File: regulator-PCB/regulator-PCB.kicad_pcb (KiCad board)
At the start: 2 copper layers, 92 parts, among them J1 Conn_ARM_SWD_TagConnect_TC2030, J2 PJ-059A, J3 Conn_01x01_Pin, J4 Conn_01x01_Pin, J5 Conn_01x01_Pin, J6 Conn_01x01_Pin, J7 Conn_01x01_Pin, Q1 2N3904, Q10 2N3904, Q11 2N3904, Q12 2N3904, Q13 2N3904, Q14 2N3904, Q15 2N3904, Q2 2N3904, Q3 2N3904, Q4 2N3904, Q5 2N3904, Q6 2N3904, Q7 2N3904, Q8 2N3904, Q9 2N3904, U1 STM32C092KCT6, U10 LH1546AT, U11 LH1546AT, U12 LH1546AT, U13 LH1546AT, U14 LH1546AT, U15 LH1546AT, U16 LH1546AT, U17 LH1546AT, U2 LP2985-3.3, U3 LH1546AT, U4 LH1546AT, U5 LH1546AT, U6 LH1546AT, U7 LH1546AT, U8 LH1546AT, U9 LH1546AT

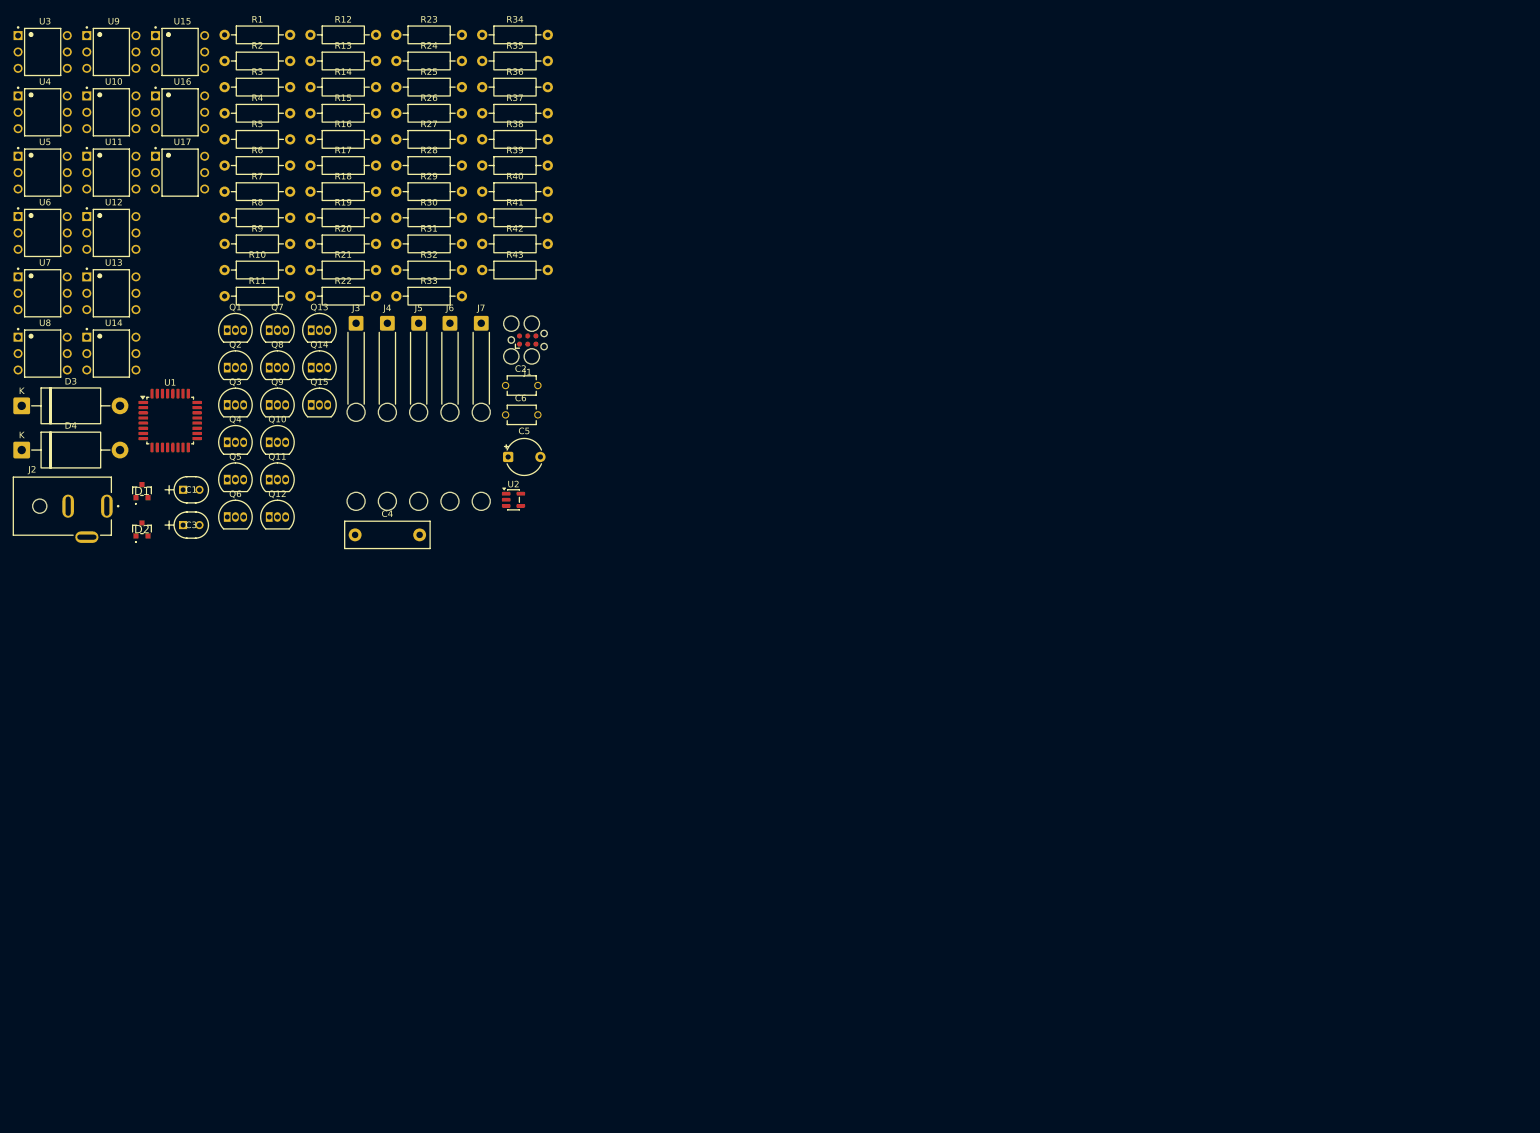
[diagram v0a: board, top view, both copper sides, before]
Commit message: Regular PCB schematic completed. Drafted a poor design for the regulator PCB, then added line voltage safety constraints. Pending PCB redesign.
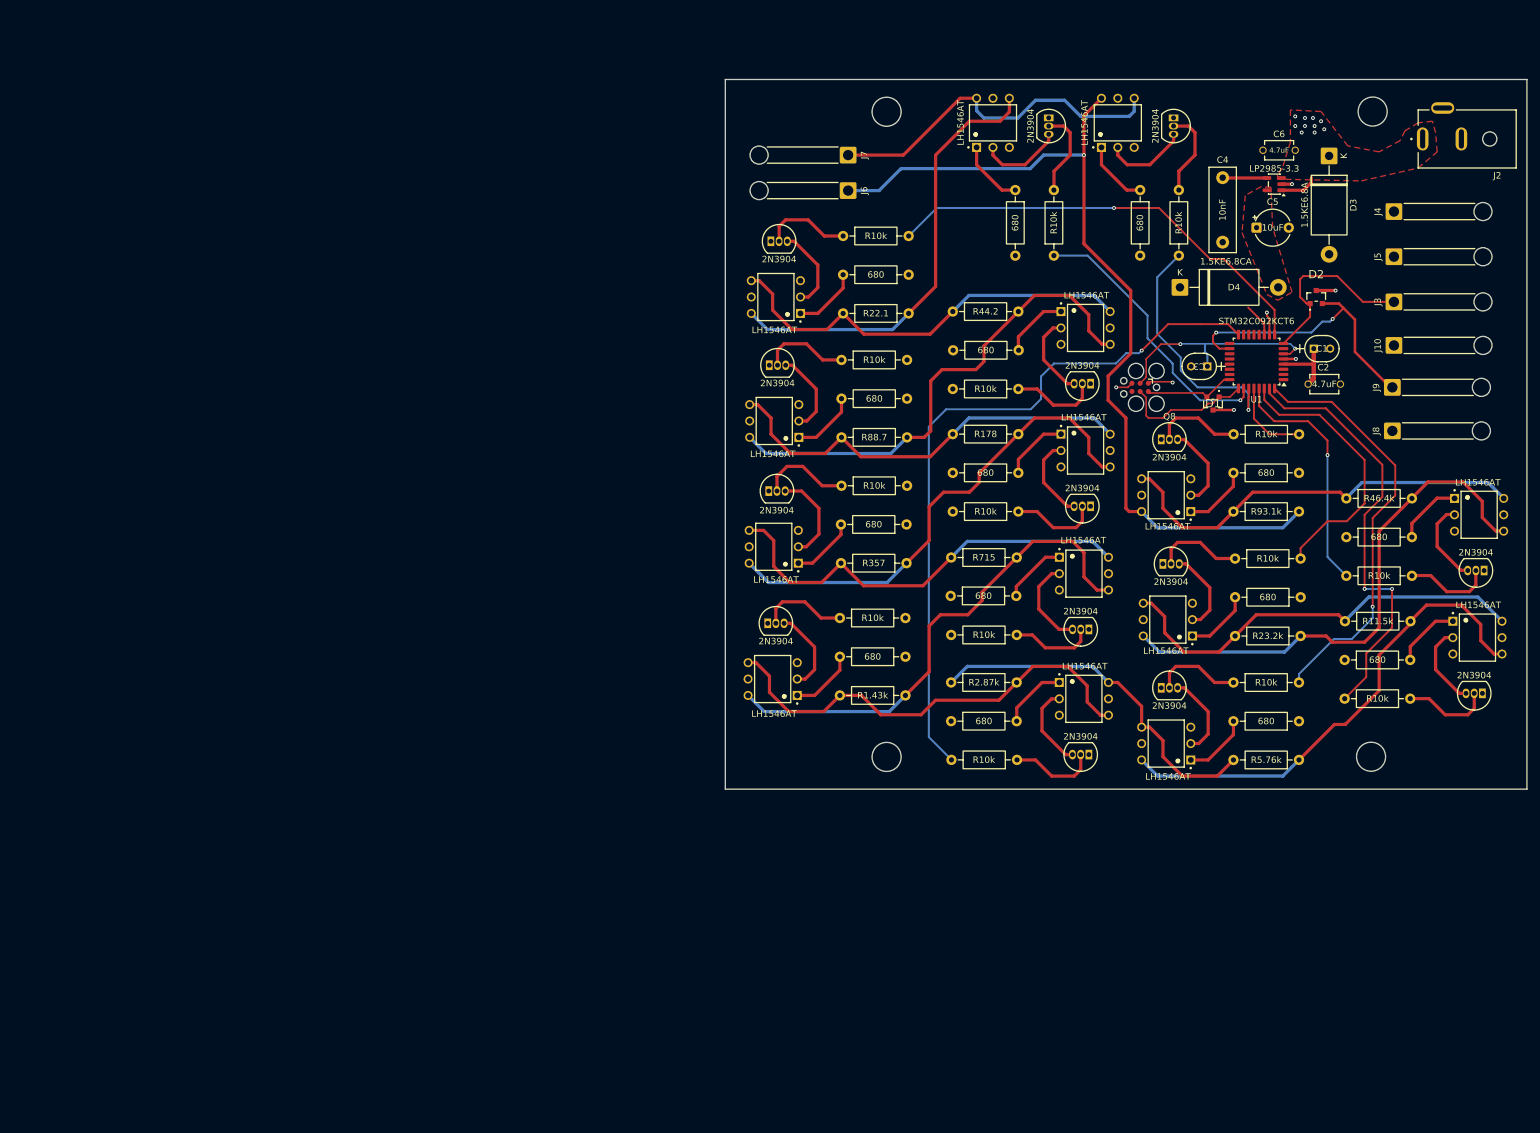
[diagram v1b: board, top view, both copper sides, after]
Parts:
- added H1: MountingHole, MountingHole:MountingHole_4.5mm, F.Cu at (229.2, 130.2)
- added H2: MountingHole, MountingHole:MountingHole_4.5mm, F.Cu at (229.5, 30.2)
- added H3: MountingHole, MountingHole:MountingHole_4.5mm, F.Cu at (154.2, 30.3)
- added H4: MountingHole, MountingHole:MountingHole_4.5mm, F.Cu at (154.2, 130.3)
- added J10: Conn_01x01_Pin, Connector_Wire:SolderWire-0.75sqmm_1x01_D1.25mm_OD2.3mm_Relief, F.Cu at (232.8, 66.5)
- added J8: Conn_01x01_Pin, Connector_Wire:SolderWire-0.75sqmm_1x01_D1.25mm_OD2.3mm_Relief, F.Cu at (232.6, 79.8)
- added J9: Conn_01x01_Pin, Connector_Wire:SolderWire-0.75sqmm_1x01_D1.25mm_OD2.3mm_Relief, F.Cu at (232.6, 73.0)
- J3, J4, J5, J6, J7: footprint Connector_Wire:SolderWire-0.5sqmm_1x01_D0.9mm_OD2.3mm_Relief2x -> Connector_Wire:SolderWire-0.75sqmm_1x01_D1.25mm_OD2.3mm_Relief
- moved U11 218.5 mm to (246.0, 92.8)
- moved U13 218.4 mm to (245.7, 111.8)
- moved J2 211.7 mm to (237.2, 34.5), turned to 180 degrees
- moved D3 206.3 mm to (222.8, 37.1), turned to -90 degrees
- moved Q11 190.9 mm to (246.5, 120.4), turned to 180 degrees
- moved Q9 190.0 mm to (246.8, 101.4), turned to 180 degrees
- moved D2 185.5 mm to (220.8, 59.0)
- moved R26 181.5 mm to (235.3, 121.2), turned to 180 degrees
- moved D4 181.3 mm to (199.6, 57.5)
- moved C1 176.6 mm to (220.4, 67.0)
- moved U12 174.4 mm to (197.8, 109.0), turned to 180 degrees
- moved U14 174.3 mm to (197.5, 128.2), turned to 180 degrees
- moved U10 173.9 mm to (197.5, 89.7), turned to 180 degrees
- moved U15 172.3 mm to (184.7, 121.3)
- moved R28 169.8 mm to (235.6, 102.2), turned to 180 degrees
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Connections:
- net /ResInput renamed /Line-R-In
- net /ResOut renamed /Line-R-Out
- net Net-(R11-Pad1) renamed /Line-R3
- net Net-(R11-Pad2) renamed /Line-R4
- net Net-(R12-Pad2) renamed /Line-R5
- net Net-(R16-Pad2) renamed /Line-R6
- net Net-(R20-Pad2) renamed /Line-R7
- net Net-(R21-Pad2) renamed /Line-R8
- net Net-(R3-Pad1) renamed /Line-R1
- net Net-(R3-Pad2) renamed /Line-R2
- net Net-(R36-Pad1) renamed /Line-R9
- net Net-(R37-Pad1) renamed /Line-R10
- net Net-(R38-Pad1) renamed /Line-R11
- net Net-(R39-Pad1) renamed /Line-R12
- net Net-(R40-Pad1) renamed /Line-R13
- D2 pad 2: unconnected-(D2-A/K_2-Pad2) -> /rotary-encoder-output
- U1 pad 18: unconnected-(U1-PA8-Pad18) -> /rotary-encoder-output
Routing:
- net +5V: track 0.00 -> 271.5 mm, vias 0 -> 10
- net /Line-R-In: track 0.00 -> 138.2 mm, vias 0 -> 1
- net /Bit7: track 0.00 -> 110.4 mm, vias 0 -> 1
- net /Line-R12: track 0.00 -> 82.0 mm
- net /Line-R7: track 0.00 -> 78.1 mm
- net /Line-R3: track 0.00 -> 77.6 mm
- net /Line-R5: track 0.00 -> 76.3 mm
- net /Line-R10: track 0.00 -> 76.0 mm
- net /Line-R8: track 0.00 -> 70.5 mm
- net /Line-R1: track 0.00 -> 69.1 mm
- net /Bit0: track 0.00 -> 68.9 mm, vias 0 -> 1
- net /Line-R6: track 0.00 -> 67.9 mm
- net /Bit9: track 0.00 -> 67.5 mm, vias 0 -> 2
- net /Line-R4: track 0.00 -> 66.3 mm
- net /Line-R11: track 0.00 -> 66.2 mm
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- added copper zone on F.Cu, net +3.3V
- added copper zone on F.Cu, net +5V
- added copper zone on In2.Cu, net +5V
- added copper zone on In1.Cu, net GND
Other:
- board outline added: 124.2 x 110 mm
- copper layers 2 -> 4

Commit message: Regulator PCB v1.0 designed and ordered.
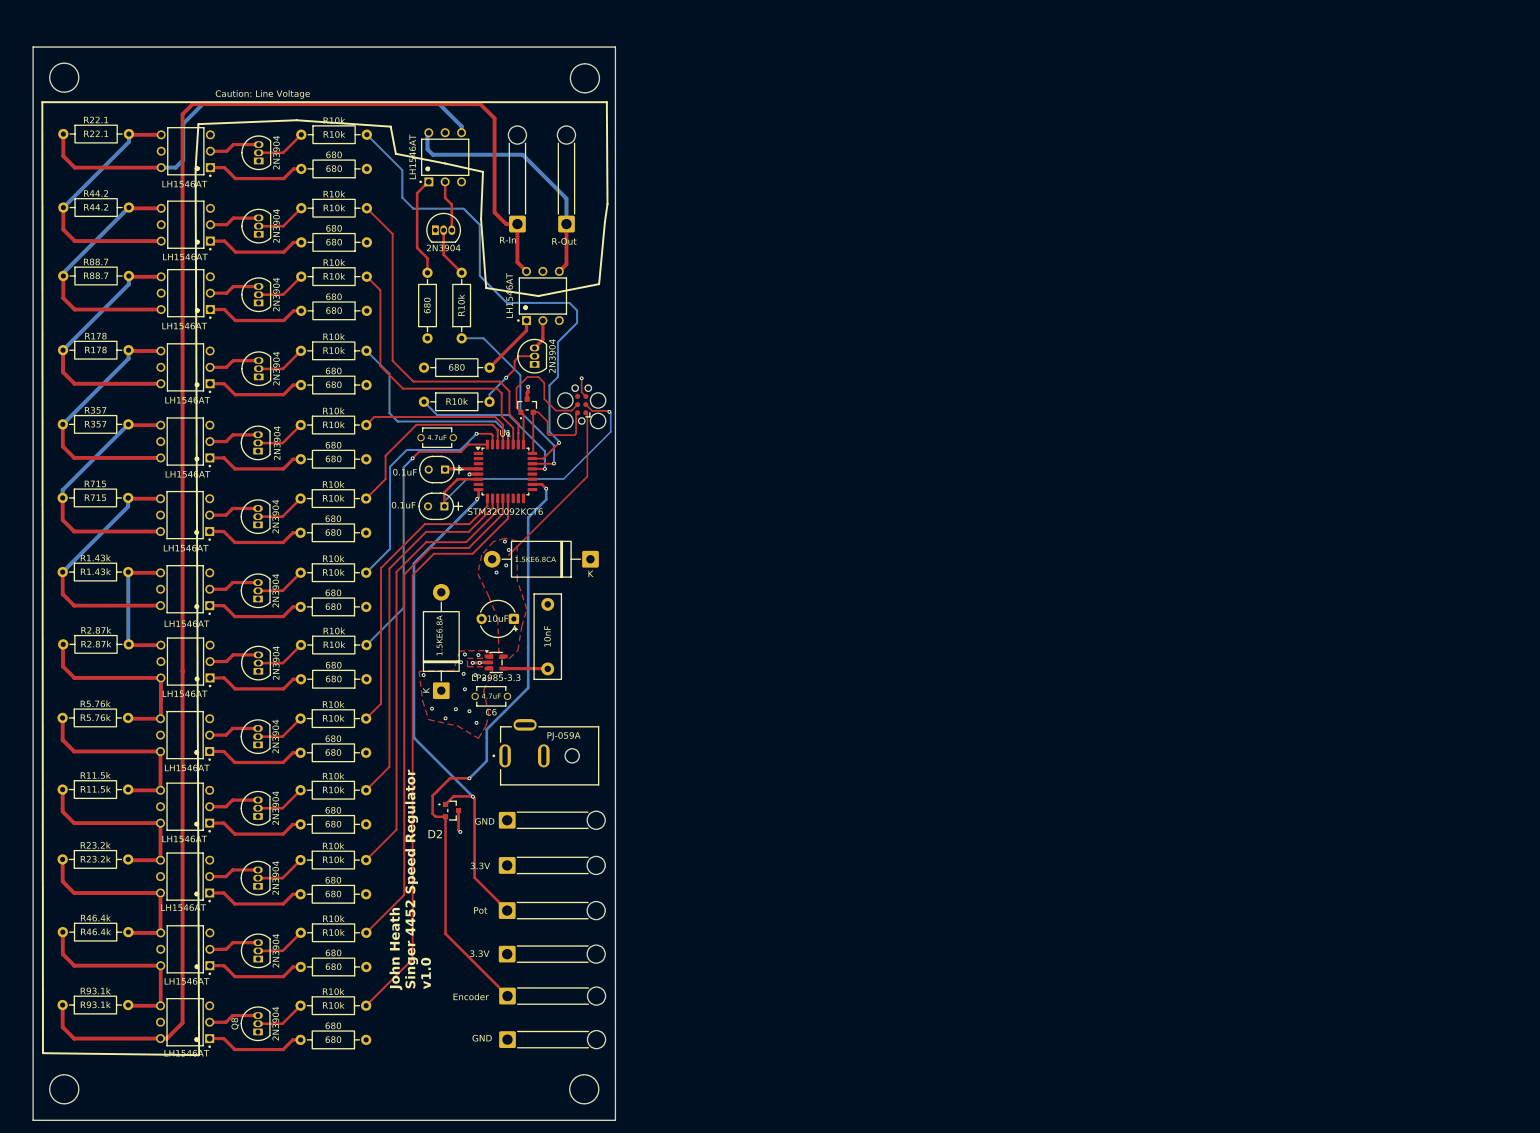
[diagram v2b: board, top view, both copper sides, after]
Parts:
- moved U11 211.5 mm to (45.5, 160.1), turned to 180 degrees
- moved R40 210.0 mm to (26.5, 157.4)
- moved R41 206.3 mm to (26.4, 168.7), turned to 0 degrees
- moved H2 202.9 mm to (26.7, 25.0)
- moved U13 202.0 mm to (45.4, 138.0), turned to 180 degrees
- moved R38 200.5 mm to (26.4, 135.3)
- moved Q9 199.3 mm to (56.8, 161.6), turned to 90 degrees
- moved H3 198.0 mm to (26.7, 181.8)
- moved R39 195.0 mm to (26.4, 146.2), turned to 0 degrees
- moved R37 191.8 mm to (26.4, 124.2), turned to 0 degrees
- moved Q11 190.7 mm to (56.7, 139.5), turned to 90 degrees
- moved R28 180.9 mm to (63.4, 157.5), turned to 0 degrees
- moved U10 172.6 mm to (45.4, 171.4)
- moved R26 172.6 mm to (63.3, 135.4), turned to 0 degrees
- moved J2 171.4 mm to (95.0, 130.1)
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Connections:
- U1 pad 10: /Bit1 -> /Bit9
- U1 pad 11: /Bit2 -> /Bit10
- U1 pad 12: /Bit3 -> /Bit11
- U1 pad 13: /Bit4 -> /Bit12
- U1 pad 14: /Bit5 -> unconnected-(U1-PA7-Pad14)
- U1 pad 15: /Bit6 -> unconnected-(U1-PB0-Pad15)
- U1 pad 16: /Bit7 -> unconnected-(U1-PB1-Pad16)
- U1 pad 21: unconnected-(U1-PA10-Pad21) -> /MinResBit
- U1 pad 22: unconnected-(U1-PA11[PA9]-Pad22) -> /MaxResBit
- U1 pad 23: unconnected-(U1-PA12[PA10]-Pad23) -> /Bit0
- U1 pad 26: /MaxResBit -> /Bit1
- U1 pad 27: /MinResBit -> /Bit2
- U1 pad 28: /Bit12 -> /Bit3
- U1 pad 29: /Bit11 -> /Bit4
- U1 pad 30: /Bit10 -> /Bit5
- U1 pad 31: /Bit9 -> /Bit6
- U1 pad 32: /Bit8 -> /Bit7
- U1 pad 9: /Bit0 -> /Bit8
- U10 pad 5: unconnected-(U10-Pad5) -> /Line-NC12
- U11 pad 5: unconnected-(U11-Pad5) -> /Line-NC11
- U12 pad 5: unconnected-(U12-Pad5) -> /Line-NC10
- U13 pad 5: unconnected-(U13-Pad5) -> /Line-NC15
- U14 pad 5: unconnected-(U14-Pad5) -> /Line-NC9
- U15 pad 5: unconnected-(U15-Pad5) -> /Line-NC8
- U16 pad 5: unconnected-(U16-Pad5) -> /Line-NC14
- U17 pad 5: unconnected-(U17-Pad5) -> /Line-NC13
- U3 pad 5: unconnected-(U3-Pad5) -> /Line-NC1
- U4 pad 5: unconnected-(U4-Pad5) -> /Line-NC2
- U5 pad 5: unconnected-(U5-Pad5) -> /Line-NC3
- U6 pad 5: unconnected-(U6-Pad5) -> /Line-NC4
- U7 pad 5: unconnected-(U7-Pad5) -> /Line-NC5
- U8 pad 5: unconnected-(U8-Pad5) -> /Line-NC6
- U9 pad 5: unconnected-(U9-Pad5) -> /Line-NC7
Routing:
- net +5V: track 271.5 -> 56.7 mm, vias 10 -> 13
- net /Line-R-In: track 138.2 -> 241.4 mm, vias 1 -> 0
- net /Bit12: track 12.7 -> 91.3 mm
- net /Bit7: track 110.4 -> 44.4 mm
- net +3.3V: track 54.0 -> 117.0 mm, vias 1 -> 5
- net /Line-R12: track 82.0 -> 30.6 mm
- net /FootPedalPotOutput: track 29.0 -> 80.2 mm, vias 0 -> 2
- net /Bit1: track 3.59 -> 54.2 mm, vias 1 -> 0
- net /Line-R8: track 70.5 -> 21.4 mm
- net /rotary-encoder-output: track 45.4 -> 94.0 mm
- net /Line-R10: track 76.0 -> 30.4 mm
- net /Bit11: track 37.7 -> 79.5 mm, vias 1 -> 0
- net /Bit2: track 5.24 -> 44.0 mm
- net /Line-R3: track 77.6 -> 39.2 mm
- net /Line-R7: track 78.1 -> 40.1 mm
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- added copper zone on In2.Cu, net +3.3V
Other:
- board size 124.2 x 110 mm -> 90.3 x 166.4 mm
- board text added: "3.3V"
- board text added: "680"
- board text added: "Caution: Line Voltage"
- board text added: "Encoder"
- board text added: "GND"
- board text added: "John Heath Singer 4452 Speed Regulator v1.0"
- board text added: "Pot"
- board text added: "R-In"
- board text added: "R-Out"
- board text added: "R1.43k"
- board text added: "R10k"
- board text added: "R11.5k"
- board text added: "R178"
- board text added: "R2.87k"
- board text added: "R22.1"
- board text added: "R23.2k"
- board text added: "R357"
- board text added: "R44.2"
- board text added: "R46.4k"
- board text added: "R5.76k"
- board text added: "R715"
- board text added: "R88.7"
- board text added: "R93.1k"
